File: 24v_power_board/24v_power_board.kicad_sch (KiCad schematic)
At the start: 50 parts, among them J1 Conn_01x02_Pin, J10 Conn_01x02_Socket, J11 Conn_01x02_Socket, J12 Conn_01x02_Socket, J13 Conn_01x02_Socket, J14 Conn_01x02_Socket, J15 Conn_01x04_Pin, J2 Conn_01x02_Pin, J3 Conn_01x02_Pin, J4 Conn_01x02_Pin, J5 Conn_01x02_Socket, J6 Conn_01x02_Socket, J7 Conn_01x02_Socket, J8 Conn_01x02_Socket, J9 Conn_01x02_Socket, K1 A31CCQ24VDC1D, Q1 2SA1015, Q2 BS170, U1 INA226

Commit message: 24V基板　テストポイントを追加，C4をセラコンに変更，ver 0.5 C4を電解コンデンサにすると，可変抵抗を高抵抗に設定した際に漏れ電流のほうが充電電流を上回る可能性があったため．
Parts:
- added TP1, TP3, TP4: TestPoint_Probe, TestPoint:TestPoint_THTPad_D2.0mm_Drill1.0mm, symbol Connector:TestPoint_Probe
- added TP2: TestPoint_2Pole, TestPoint:TestPoint_2Pads_Pitch2.54mm_Drill0.8mm, symbol Connector:TestPoint_2Pole
- C4: footprint Capacitor_THT:CP_Radial_D5.0mm_P2.00mm -> Capacitor_THT:C_Disc_D6.0mm_W4.4mm_P5.00mm; symbol Device:C_Polarized -> Device:C; Buy_URL https://akizukidenshi.com/catalog/g/g117897/ -> https://akizukidenshi.com/catalog/g/g108155/
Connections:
- net +24V_CTRL: now also TP4.1
- net +24V_DRV: now also TP3.1
- net GND: now also TP2.1, TP2.2
- net at C4.1, D4.2 (A), DZ1.1 (K)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: now also TP1.1
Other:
- note added: "なるべくネットタイの近くに配置"
- moved on the sheet: D3, DZ1, Q1, Q2, R10, R6, R7, R8

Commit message: 24V基板　シルクの一部修正，ver 1.0
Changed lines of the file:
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@@
 	(text "24Vフロントエンド"
 		(exclude_from_sim no)
-		(at 236.474 18.288 0)
+		(at 247.142 18.034 0)
 		(effects
 			(font

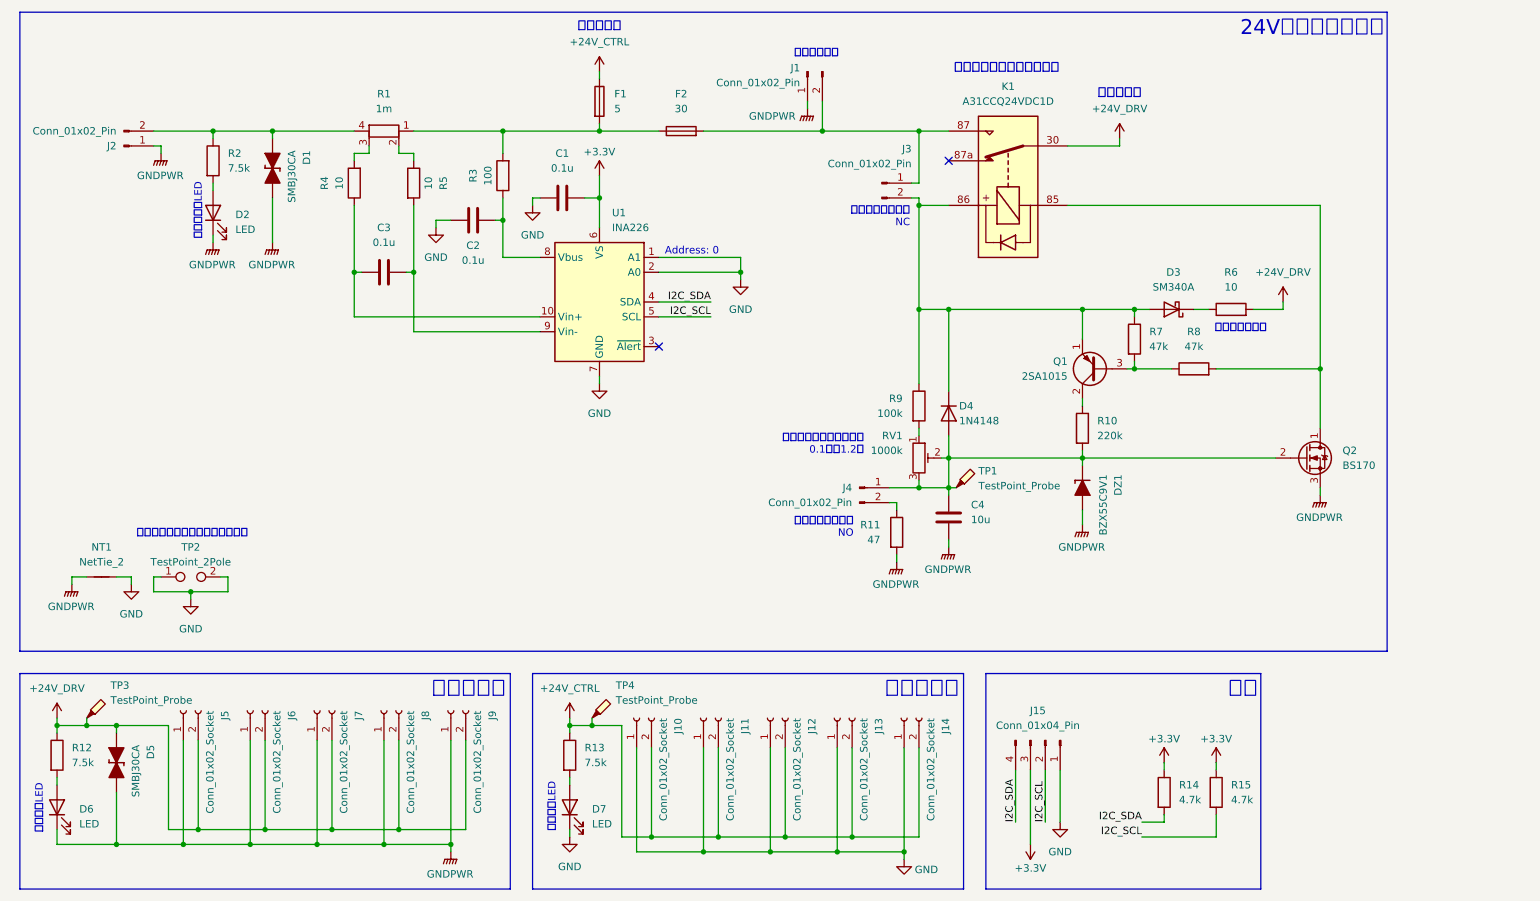
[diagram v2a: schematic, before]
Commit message: 24V電源基板　プリチャージ抵抗と直列にポリスイッチを追加，ver 1.2 非常停止スイッチ接続端子がどちらもONになった場合，リレーがオンにならず，プリチャージ抵抗に電流が流れ続ける可能性があった．そこでポリスイッチを直列に接続することで，プリチャージ抵抗に電流が流れ続けた場合に電流が遮断されるようにした．
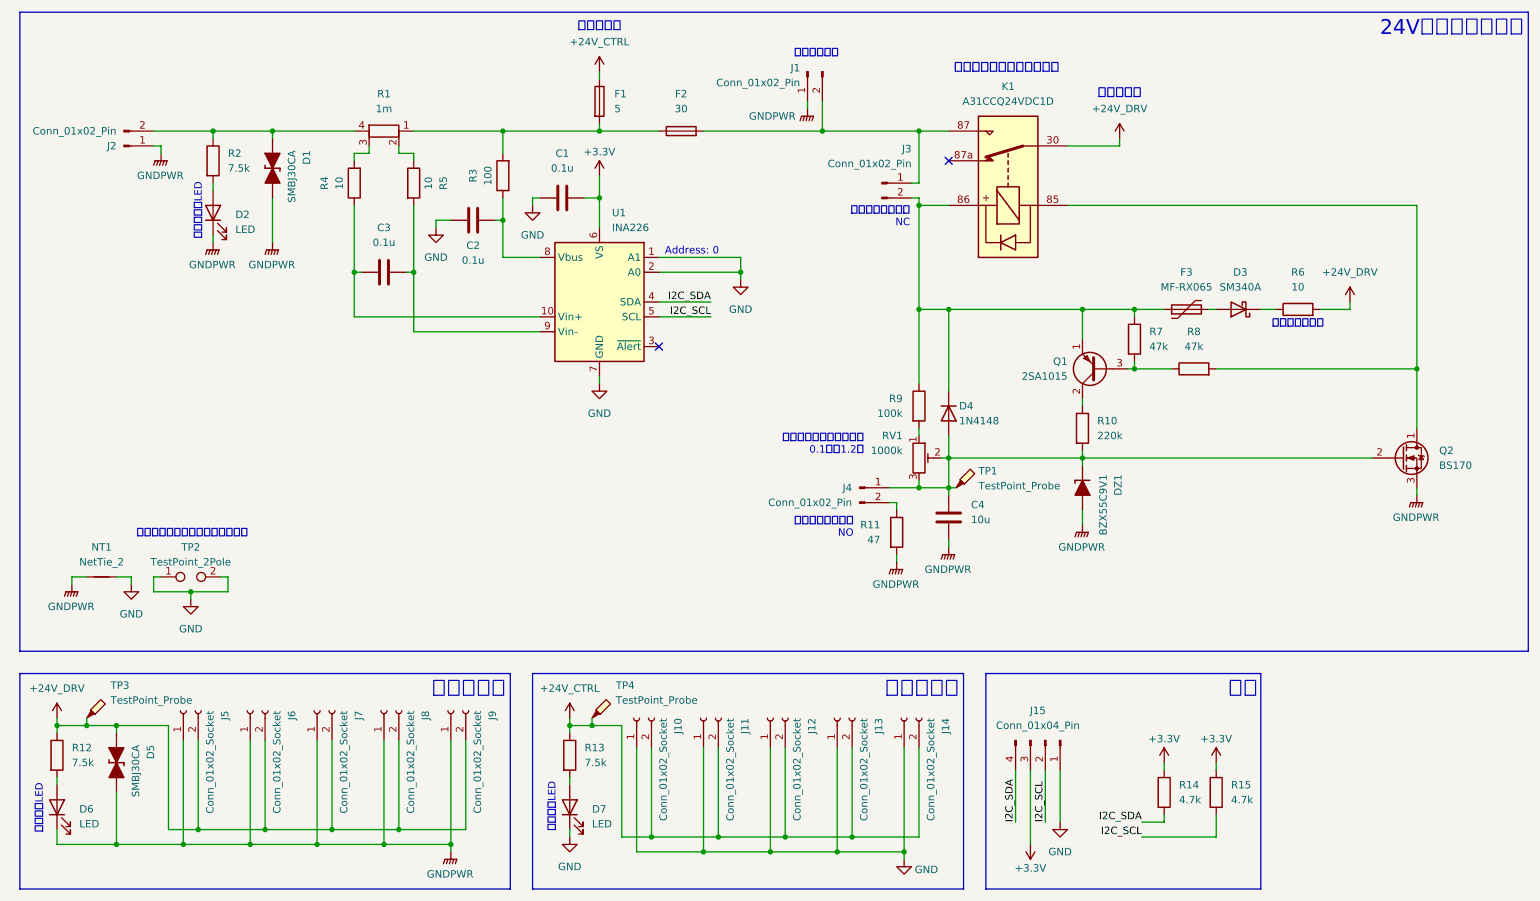
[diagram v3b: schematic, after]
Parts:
- added F3: MF-RX065, Fuse:Fuse_BelFuse_0ZRE0016FF_L9.9mm_W3.8mm, symbol Device:Polyfuse
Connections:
- net at D4.1 (K), J3.2 (Pin_2), K1.86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: now also F3.1; no longer D3.2 (A)
- new net: D3.2 (A), F3.2
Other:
- moved on the sheet: D3, Q2, R6
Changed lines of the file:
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@@
 	(rectangle
 		(start 13.97 15.24)
-		(end 247.65 124.46)
+		(end 271.78 124.46)
 		(stroke
 			(width 0)
@@
 	(text "24Vフロントエンド"
 		(exclude_from_sim no)
-		(at 247.142 18.034 0)
+		(at 271.018 18.034 0)
 		(effects
 			(font
@@
 	(text "プリチャージ用"
 		(exclude_from_sim no)
-		(at 218.186 68.58 0)
+		(at 232.41 67.818 0)
 		(effects
 			(font
 				(size 1.27 1.27)
 			)
-			(justify left top)
+			(justify top)
 		)
 	)
@@
 	)
 	(junction
-		(at 236.22 76.2)
+		(at 252.73 76.2)
 		(diameter 0)
 		(color 0 0 0 0)
@@
 	(wire
 		(pts
-			(xy 218.44 76.2) (xy 236.22 76.2)
-		)
-		(stroke
-			(width 0)
-			(type default)
-		)
-	)
-	(wire
-		(pts
-			(xy 236.22 96.52) (xy 236.22 97.79)
+			(xy 252.73 96.52) (xy 252.73 97.79)
 		)
 		(stroke
@@
 	(wire
 		(pts
-			(xy 172.72 91.44) (xy 228.6 91.44)
+			(xy 172.72 91.44) (xy 245.11 91.44)
 		)
 		(stroke
@@
 	(wire
 		(pts
-			(xy 214.63 66.04) (xy 217.17 66.04)
+			(xy 226.06 66.04) (xy 228.6 66.04)
 		)
 		(stroke
@@
 	(wire
 		(pts
-			(xy 193.04 48.26) (xy 236.22 48.26)
+			(xy 193.04 48.26) (xy 252.73 48.26)
 		)
 		(stroke
@@
 	(wire
 		(pts
-			(xy 224.79 66.04) (xy 229.87 66.04)
+			(xy 236.22 66.04) (xy 241.3 66.04)
 		)
 		(stroke
@@
 	(wire
 		(pts
+			(xy 218.44 76.2) (xy 252.73 76.2)
+		)
+		(stroke
+			(width 0)
+			(type default)
+		)
+	)
+	(wire
+		(pts
+			(xy 217.17 66.04) (xy 218.44 66.04)
+		)
+		(stroke
+			(width 0)
+			(type default)
+		)
+	)
+	(wire
+		(pts
 			(xy 53.34 139.7) (xy 53.34 157.48)
 		)
@@
 	(wire
 		(pts
-			(xy 204.47 66.04) (xy 207.01 66.04)
+			(xy 204.47 66.04) (xy 209.55 66.04)
 		)
 		(stroke
@@
 	(wire
 		(pts
-			(xy 236.22 76.2) (xy 236.22 86.36)
+			(xy 252.73 76.2) (xy 252.73 86.36)
 		)
 		(stroke
@@
 	(wire
 		(pts
-			(xy 236.22 48.26) (xy 236.22 76.2)
+			(xy 252.73 48.26) (xy 252.73 76.2)
 		)
 		(stroke
@@
 	(wire
 		(pts
-			(xy 229.87 66.04) (xy 229.87 64.77)
+			(xy 241.3 66.04) (xy 241.3 64.77)
 		)
 		(stroke
@@
 	(symbol
 		(lib_id "power:GNDPWR")
-		(at 236.22 97.79 0)
+		(at 252.73 97.79 0)
 		(unit 1)
 		(body_style 1)
@@
 		(fields_autoplaced yes)
 		(property "Reference" "#PWR013"
-			(at 236.22 102.87 0)
+			(at 252.73 102.87 0)
 			(hide yes)
 			(show_name no)
@@
 		)
 		(property "Value" "GNDPWR"
-			(at 236.093 101.6 0)
+			(at 252.603 101.6 0)
 			(show_name no)
 			(do_not_autoplace no)
@@
 		)
 		(property "Footprint" ""
-			(at 236.22 99.06 0)
+			(at 252.73 99.06 0)
 			(hide yes)
 			(show_name no)
@@
 		)
 		(property "Datasheet" ""
-			(at 236.22 99.06 0)
+			(at 252.73 99.06 0)
 			(hide yes)
 			(show_name no)
@@
 		)
 		(property "Description" "Power symbol creates a global label with name \"GNDPWR\" , global ground"
-			(at 236.22 97.79 0)
+			(at 252.73 97.79 0)
 			(hide yes)
 			(show_name no)
@@
 	(symbol
 		(lib_id "power:+24V")
-		(at 229.87 64.77 0)
+		(at 241.3 64.77 0)
 		(unit 1)
 		(body_style 1)
@@
 		(fields_autoplaced yes)
 		(property "Reference" "#PWR011"
-			(at 229.87 68.58 0)
+			(at 241.3 68.58 0)
 			(hide yes)
 			(show_name no)
@@
 		)
 		(property "Value" "+24V_DRV"
-			(at 229.87 59.69 0)
+			(at 241.3 59.69 0)
 			(show_name no)
 			(do_not_autoplace no)
@@
 		)
 		(property "Footprint" ""
-			(at 229.87 64.77 0)
+			(at 241.3 64.77 0)
 			(hide yes)
 			(show_name no)
@@
 		)
 		(property "Datasheet" ""
-			(at 229.87 64.77 0)
+			(at 241.3 64.77 0)
 			(hide yes)
 			(show_name no)
@@
 		)
 		(property "Description" "Power symbol creates a global label with name \"+24V\""
-			(at 229.87 64.77 0)
+			(at 241.3 64.77 0)
 			(hide yes)
 			(show_name no)
@@
 	)
 	(symbol
+		(lib_id "Device:Polyfuse")
+		(at 213.36 66.04 90)
+		(unit 1)
+		(body_style 1)
+		(exclude_from_sim no)
+		(in_bom yes)
+		(on_board yes)
+		(in_pos_files yes)
+		(dnp no)
+		(fields_autoplaced yes)
+		(property "Reference" "F3"
+			(at 213.36 59.69 90)
+			(show_name no)
+			(do_not_autoplace no)
+			(effects
+				(font
+					(size 1.27 1.27)
+				)
+			)
+		)
+		(property "Value" "MF-RX065"
+			(at 213.36 62.23 90)
+			(show_name no)
+			(do_not_autoplace no)
+			(effects
+				(font
+					(size 1.27 1.27)
+				)
+			)
+		)
+		(property "Footprint" "Fuse:Fuse_BelFuse_0ZRE0016FF_L9.9mm_W3.8mm"
+			(at 218.44 64.77 0)
+			(hide yes)
+			(show_name no)
+			(do_not_autoplace no)
+			(effects
+				(font
+					(size 1.27 1.27)
+				)
+				(justify left)
+			)
+		)
+		(property "Datasheet" ""
+			(at 213.36 66.04 0)
+			(hide yes)
+			(show_name no)
+			(do_not_autoplace no)
+			(effects
+				(font
+					(size 1.27 1.27)
+				)
+			)
+		)
+		(property "Description" "Resettable fuse, polymeric positive temperature coefficient"
+			(at 213.36 66.04 0)
+			(hide yes)
+			(show_name no)
+			(do_not_autoplace no)
+			(effects
+				(font
+					(size 1.27 1.27)
+				)
+			)
+		)
+		(pin "2"
+		)
+		(pin "1"
+		)
+		(instances
+			(project "24v_power_board"
+				(path "/7e933acb-f512-46a3-a247-cbd9deaf4ead"
+					(reference "F3")
+					(unit 1)
+				)
+			)
+		)
+	)
+	(symbol
 		(lib_id "Connector:Conn_01x02_Socket")
 		(at 76.2 134.62 90)
@@
 	(symbol
 		(lib_id "Device:D_Schottky")
-		(at 210.82 66.04 180)
+		(at 222.25 66.04 180)
 		(unit 1)
 		(body_style 1)
@@
 		(fields_autoplaced yes)
 		(property "Reference" "D3"
-			(at 211.1375 59.69 0)
+			(at 222.5675 59.69 0)
 			(show_name no)
 			(do_not_autoplace no)
@@
 		)
 		(property "Value" "SM340A"
-			(at 211.1375 62.23 0)
+			(at 222.5675 62.23 0)
 			(show_name no)
 			(do_not_autoplace no)
@@
 		)
 		(property "Footprint" "Diode_SMD:D_SMA_Handsoldering"
-			(at 210.82 66.04 0)
+			(at 222.25 66.04 0)
 			(hide yes)
 			(show_name no)
@@
 		)
 		(property "Datasheet" ""
-			(at 210.82 66.04 0)
+			(at 222.25 66.04 0)
 			(hide yes)
 			(show_name no)
@@
 		)
 		(property "Description" "Schottky diode"
-			(at 210.82 66.04 0)
+			(at 222.25 66.04 0)
 			(hide yes)
 			(show_name no)
@@
 		)
 		(property "Buy_URL" "https://akizukidenshi.com/catalog/g/g109915/"
-			(at 210.82 66.04 0)
+			(at 222.25 66.04 0)
 			(hide yes)
 			(show_name no)
@@
 	(symbol
 		(lib_id "Transistor_FET:BS170")
-		(at 233.68 91.44 0)
+		(at 250.19 91.44 0)
 		(unit 1)
 		(body_style 1)
@@
 		(fields_autoplaced yes)
 		(property "Reference" "Q2"
-			(at 240.03 90.1699 0)
+			(at 256.54 90.1699 0)
 			(show_name no)
 			(do_not_autoplace no)
@@
 		)
 		(property "Value" "BS170"
-			(at 240.03 92.7099 0)
+			(at 256.54 92.7099 0)
 			(show_name no)
 			(do_not_autoplace no)
@@
 		)
 		(property "Footprint" "Package_TO_SOT_THT:TO-92_Inline"
-			(at 238.76 93.345 0)
+			(at 255.27 93.345 0)
 			(hide yes)
 			(show_name no)
@@
 		)
 		(property "Datasheet" "https://www.onsemi.com/pub/Collateral/BS170-D.PDF"
-			(at 238.76 95.25 0)
+			(at 255.27 95.25 0)
 			(hide yes)
 			(show_name no)
@@
 		)
 		(property "Description" "0.5A Id, 60V Vds, N-Channel MOSFET, TO-92"
-			(at 233.68 91.44 0)
+			(at 250.19 91.44 0)
 			(hide yes)
 			(show_name no)
@@
 		)
 		(property "Buy_URL" "https://akizukidenshi.com/catalog/g/g109724/"
-			(at 233.68 91.44 0)
+			(at 250.19 91.44 0)
 			(hide yes)
 			(show_name no)
@@
 	(symbol
 		(lib_id "Device:R")
-		(at 220.98 66.04 90)
+		(at 232.41 66.04 90)
 		(unit 1)
 		(body_style 1)
@@
 		(fields_autoplaced yes)
 		(property "Reference" "R6"
-			(at 220.98 59.69 90)
+			(at 232.41 59.69 90)
 			(show_name no)
 			(do_not_autoplace no)
@@
 		)
 		(property "Value" "10"
-			(at 220.98 62.23 90)
+			(at 232.41 62.23 90)
 			(show_name no)
 			(do_not_autoplace no)
@@
 		)
 		(property "Footprint" "Resistor_THT:R_Axial_Power_L25.0mm_W9.0mm_P7.62mm_Vertical"
-			(at 220.98 67.818 90)
+			(at 232.41 67.818 90)
 			(hide yes)
 			(show_name no)
@@
 		)
 		(property "Datasheet" ""
-			(at 220.98 66.04 0)
+			(at 232.41 66.04 0)
 			(hide yes)
 			(show_name no)
@@
 		)
 		(property "Description" "5W10Ω"
-			(at 220.98 66.04 0)
+			(at 232.41 66.04 0)
 			(hide yes)
 			(show_name no)
@@
 		)
 		(property "Fuse" ""
-			(at 220.98 66.04 90)
+			(at 232.41 66.04 90)
 			(hide yes)
 			(show_name no)
@@
 		)
 		(property "MPN_URL" ""
-			(at 220.98 66.04 90)
+			(at 232.41 66.04 90)
 			(hide yes)
 			(show_name no)
@@
 		)
 		(property "Buy_URL" "https://akizukidenshi.com/catalog/g/g103991/"
-			(at 220.98 66.04 90)
+			(at 232.41 66.04 90)
 			(hide yes)
 			(show_name no)

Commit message: 24V電源基板　ポリスイッチを変更，ver 1.3 変更前のポリスイッチはトリップ電流や時間が大きく，電流が遮断される前にプリチャージ抵抗や基板にダメージが入る可能性があった．そのため，トリップ電流や時間が小さいものに変更した．
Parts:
- F3: value MF-RX065 -> MF-RX030; footprint Fuse:Fuse_BelFuse_0ZRE0016FF_L9.9mm_W3.8mm -> Fuse:Fuse_Bourns_MF-RHT050; Buy_URL (none) -> https://akizukidenshi.com/catalog/g/g113076/
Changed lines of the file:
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@@
 			)
 		)
-		(property "Value" "MF-RX065"
+		(property "Value" "MF-RX030"
 			(at 213.36 62.23 90)
 			(show_name no)
@@
 			)
 		)
-		(property "Footprint" "Fuse:Fuse_BelFuse_0ZRE0016FF_L9.9mm_W3.8mm"
+		(property "Footprint" "Fuse:Fuse_Bourns_MF-RHT050"
 			(at 218.44 64.77 0)
 			(hide yes)
@@
 			(hide yes)
 			(show_name no)
+			(do_not_autoplace no)
+			(effects
+				(font
+					(size 1.27 1.27)
+				)
+			)
+		)
+		(property "Buy_URL" "https://akizukidenshi.com/catalog/g/g113076/"
+			(at 213.36 66.04 90)
+			(hide yes)
+			(show_name no)
